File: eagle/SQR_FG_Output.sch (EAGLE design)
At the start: 35 parts, among them IC1 MEGA328P, IC2 NJM7032, IC3 7805T, IC4 TLV1117-33, Q1 16MHz, T1 2SK4017, T2 2SK4017

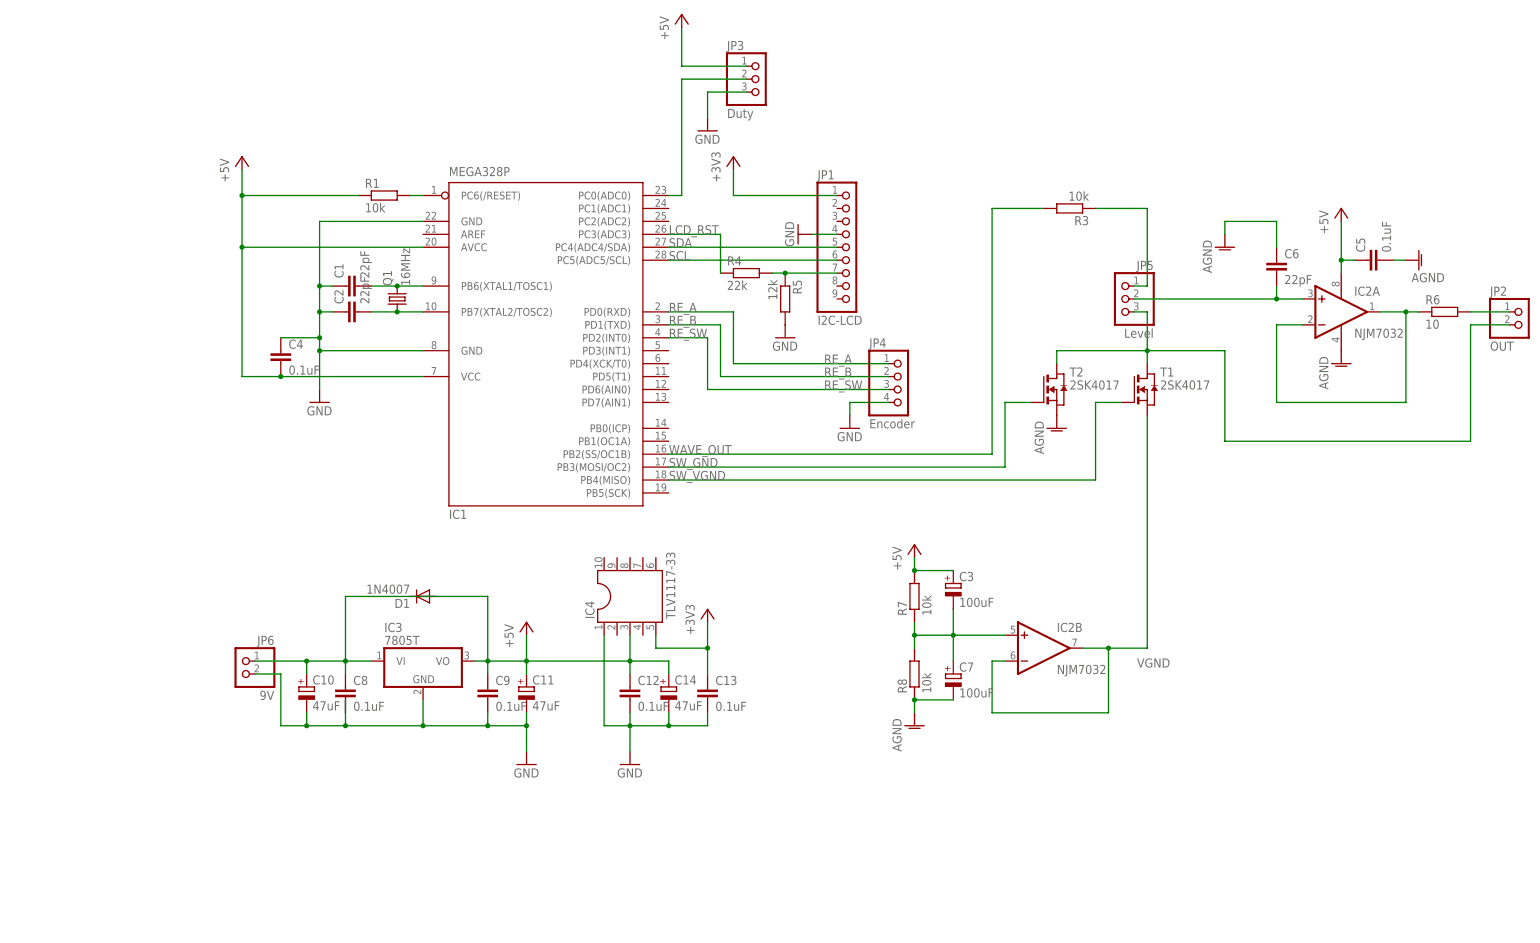
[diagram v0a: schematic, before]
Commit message: eagle files: デジタル部と出力部に基板を分割
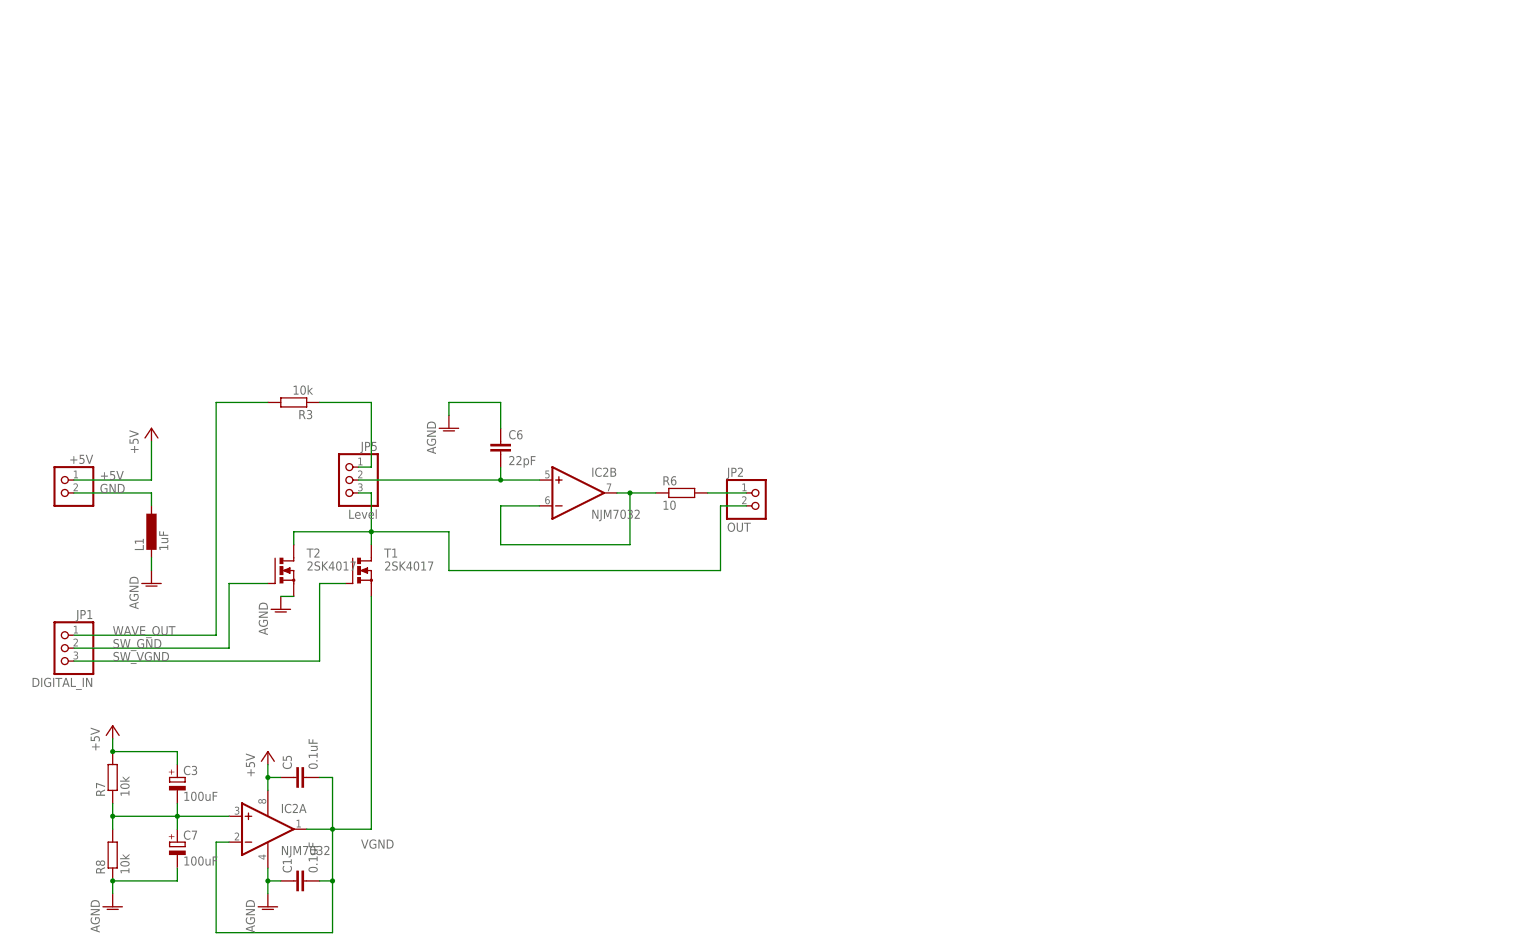
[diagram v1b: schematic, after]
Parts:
- removed C10, C11, C14: 47uF, rcl:CPOL-EUTT2D5L
- removed C12, C13, C4, C8, C9: 0.1uF, rcl:C-EU025-024X044
- removed C2: 22pF, rcl:C-EU025-024X044
- removed D1: 1N4007, diode:1N4004
- removed IC1: MEGA328P, atmel:MEGA8-P
- removed IC3: 7805T, linear:7805T
- removed IC4: TLV1117-33, ic-package:DIL10
- removed JP3: Duty, pinhead:PINHD-1X3
- removed JP4: Encoder, pinhead:PINHD-1X4
- removed JP6: 9V, pinhead:PINHD-1X2
- removed Q1: 16MHz, crystal:CRYSTALHC49S
- removed R1: 10k, rcl:R-EU_0207/7
- removed R4: 22k, rcl:R-EU_0207/7
- removed R5: 12k, rcl:R-EU_0207/7
- added +5V: (no value), pinhead:PINHD-1X2
- added L1: 1uF, rcl:L-EU0204/7
- C1: value 22pF -> 0.1uF
- JP1: value I2C-LCD -> DIGITAL_IN; device pinhead:PINHD-1X9 -> pinhead:PINHD-1X3
- T1, T2: device zetex:NMOSE3L -> transistor-power:RD06HVF1
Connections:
- removed net +3V3: C13.1, IC4.5, JP1.1
- removed net LCD_RST: IC1.PC3(ADC3), R4.1
- removed net N$1: C1.2, IC1.PB6(XTAL1/TOSC1), Q1.2
- removed net N$2: C2.2, IC1.PB7(XTAL2/TOSC2), Q1.1
- removed net N$3: IC1.PC6(/RESET), R1.2
- removed net N$9: IC1.PC0(ADC0), JP3.2
- removed net RE_A: IC1.PD0(RXD), JP4.1
- removed net RE_B: IC1.PD1(TXD), JP4.2
- removed net RE_SW: IC1.PD2(INT0), JP4.3
- removed net RST: JP1.7, R4.2, R5.1
- removed net SCL: IC1.PC5(ADC5/SCL), JP1.6
- removed net SDA: IC1.PC4(ADC4/SDA), JP1.5
- net +5V: now also +5V.1; no longer C10.+, C11.+, C12.1, C14.+, C4.2, C8.1, C9.1, IC1.AVCC, IC1.VCC@1, IC3.VI, IC3.VO, IC4.3, JP3.1, JP6.1, R1.1
- net AGND: now also C1.1, L1.2; no longer C5.2
- net GND: now also +5V.2, L1.1; no longer C1.1, C10.-, C11.-, C12.2, C13.2, C14.-, C2.1, C4.1, C8.2, C9.2, IC1.GND, IC1.GND@1, IC3.GND, IC4.1, JP1.4, JP3.3, JP4.4, JP6.2, R5.2
- net N$15: now also IC2B.+IN; no longer IC2A.+IN
- net N$16: now also IC2B.-IN, IC2B.OUT; no longer IC2A.-IN, IC2A.OUT
- net N$17: now also IC2A.+IN; no longer IC2B.+IN
- net SW_GND: now also JP1.2; no longer IC1.PB3(MOSI/OC2)
- net SW_VGND: now also JP1.3; no longer IC1.PB4(MISO)
- net VGND: now also C1.2, C5.2, IC2A.-IN, IC2A.OUT; no longer IC2B.-IN, IC2B.OUT
- net WAVE_OUT: now also JP1.1; no longer IC1.PB2(SS/OC1B)
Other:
- moved on the sheet: C1, C3, C5, C6, C7, IC2A, IC2B, JP2, JP5, R3, R6, R7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

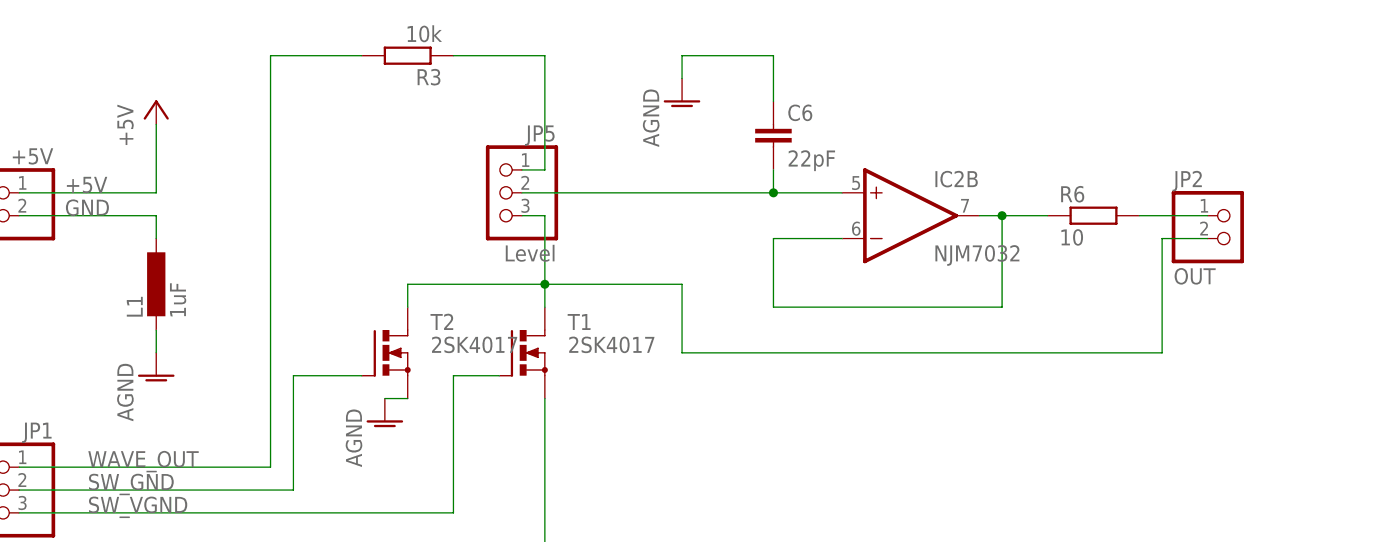
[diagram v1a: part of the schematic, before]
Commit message: SQR_FG_Digital: I2Cの信号をピンソケットで出力できるように変更
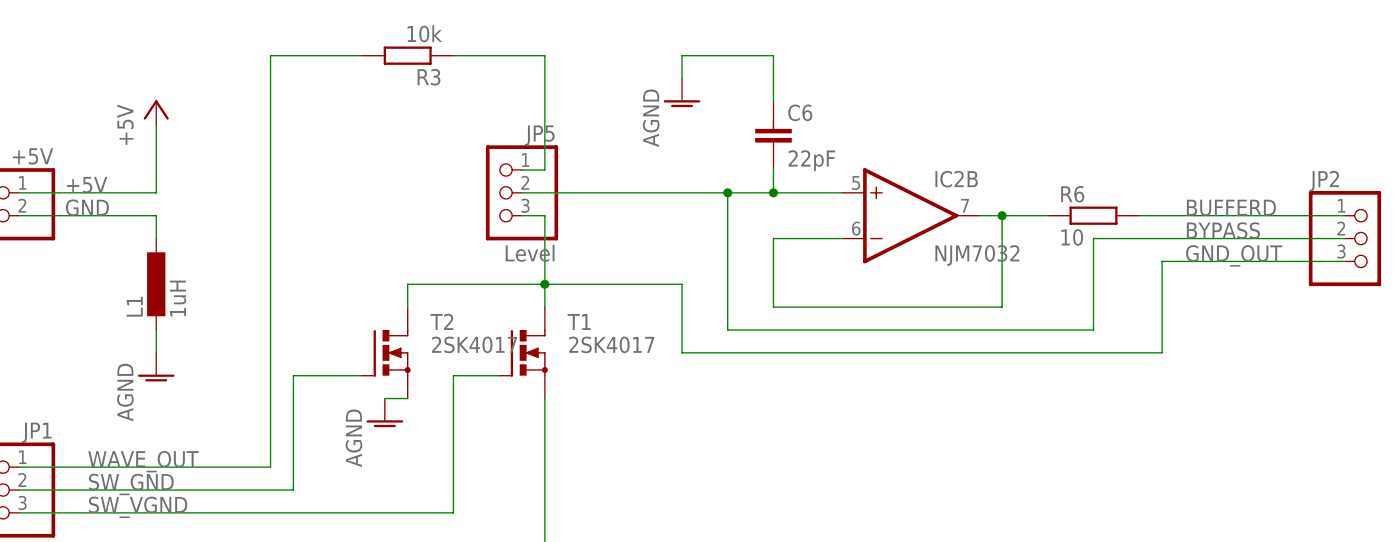
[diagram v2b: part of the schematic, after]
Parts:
- JP2: value OUT -> (none); device pinhead:PINHD-1X2 -> pinhead:PINHD-1X3
- L1: value 1uF -> 1uH
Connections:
- net N$11 renamed BUFFERD
- removed net N$15: C6.2, IC2B.+IN, JP5.2
- removed net N$6: JP2.2, JP5.3, T1.D, T2.D
- new net BYPASS: C6.2, IC2B.+IN, JP2.2, JP5.2
- new net GND_OUT: JP2.3, JP5.3, T1.D, T2.D
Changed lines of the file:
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@@
 <grid distance="0.1" unitdist="inch" unit="inch" style="dots" multiple="1" display="yes" altdistance="0.01" altunitdist="inch" altunit="inch"/>
 <layers>
-<layer number="1" name="Top" color="4" fill="1" visible="yes" active="no"/>
-<layer number="16" name="Bottom" color="1" fill="1" visible="yes" active="no"/>
-<layer number="17" name="Pads" color="2" fill="1" visible="yes" active="no"/>
-<layer number="18" name="Vias" color="2" fill="1" visible="yes" active="no"/>
-<layer number="19" name="Unrouted" color="6" fill="1" visible="yes" active="no"/>
-<layer number="20" name="Dimension" color="15" fill="1" visible="yes" active="no"/>
-<layer number="21" name="tPlace" color="7" fill="1" visible="yes" active="no"/>
-<layer number="22" name="bPlace" color="7" fill="1" visible="yes" active="no"/>
-<layer number="23" name="tOrigins" color="15" fill="1" visible="yes" active="no"/>
-<layer number="24" name="bOrigins" color="15" fill="1" visible="yes" active="no"/>
-<layer number="25" name="tNames" color="7" fill="1" visible="yes" active="no"/>
-<layer number="26" name="bNames" color="7" fill="1" visible="yes" active="no"/>
-<layer number="27" name="tValues" color="7" fill="1" visible="yes" active="no"/>
-<layer number="28" name="bValues" color="7" fill="1" visible="yes" active="no"/>
+<layer number="1" name="Top" color="4" fill="1" visible="no" active="no"/>
+<layer number="16" name="Bottom" color="1" fill="1" visible="no" active="no"/>
+<layer number="17" name="Pads" color="2" fill="1" visible="no" active="no"/>
+<layer number="18" name="Vias" color="2" fill="1" visible="no" active="no"/>
+<layer number="19" name="Unrouted" color="6" fill="1" visible="no" active="no"/>
+<layer number="20" name="Dimension" color="15" fill="1" visible="no" active="no"/>
+<layer number="21" name="tPlace" color="7" fill="1" visible="no" active="no"/>
+<layer number="22" name="bPlace" color="7" fill="1" visible="no" active="no"/>
+<layer number="23" name="tOrigins" color="15" fill="1" visible="no" active="no"/>
+<layer number="24" name="bOrigins" color="15" fill="1" visible="no" active="no"/>
+<layer number="25" name="tNames" color="7" fill="1" visible="no" active="no"/>
+<layer number="26" name="bNames" color="7" fill="1" visible="no" active="no"/>
+<layer number="27" name="tValues" color="7" fill="1" visible="no" active="no"/>
+<layer number="28" name="bValues" color="7" fill="1" visible="no" active="no"/>
 <layer number="29" name="tStop" color="7" fill="3" visible="no" active="no"/>
 <layer number="30" name="bStop" color="7" fill="6" visible="no" active="no"/>
@@
 <layer number="35" name="tGlue" color="7" fill="4" visible="no" active="no"/>
 <layer number="36" name="bGlue" color="7" fill="5" visible="no" active="no"/>
-<layer number="37" name="tTest" color="7" fill="1" visible="yes" active="no"/>
-<layer number="38" name="bTest" color="7" fill="1" visible="yes" active="no"/>
+<layer number="37" name="tTest" color="7" fill="1" visible="no" active="no"/>
+<layer number="38" name="bTest" color="7" fill="1" visible="no" active="no"/>
 <layer number="39" name="tKeepout" color="4" fill="11" visible="no" active="no"/>
 <layer number="40" name="bKeepout" color="1" fill="11" visible="no" active="no"/>
@@
 <layer number="44" name="Drills" color="7" fill="1" visible="no" active="no"/>
 <layer number="45" name="Holes" color="7" fill="1" visible="no" active="no"/>
-<layer number="46" name="Milling" color="3" fill="1" visible="yes" active="no"/>
-<layer number="47" name="Measures" color="7" fill="1" visible="yes" active="no"/>
-<layer number="48" name="Document" color="7" fill="1" visible="yes" active="no"/>
-<layer number="49" name="Reference" color="7" fill="1" visible="yes" active="no"/>
-<layer number="51" name="tDocu" color="7" fill="1" visible="yes" active="no"/>
-<layer number="52" name="bDocu" color="7" fill="1" visible="yes" active="no"/>
+<layer number="46" name="Milling" color="3" fill="1" visible="no" active="no"/>
+<layer number="47" name="Measures" color="7" fill="1" visible="no" active="no"/>
+<layer number="48" name="Document" color="7" fill="1" visible="no" active="no"/>
+<layer number="49" name="Reference" color="7" fill="1" visible="no" active="no"/>
+<layer number="51" name="tDocu" color="7" fill="1" visible="no" active="no"/>
+<layer number="52" name="bDocu" color="7" fill="1" visible="no" active="no"/>
 <layer number="90" name="Modules" color="5" fill="1" visible="yes" active="yes"/>
 <layer number="91" name="Nets" color="2" fill="1" visible="yes" active="yes"/>
@@
 <part name="T2" library="transistor-power" deviceset="RD06HVF1" device="" value="2SK4017"/>
 <part name="C5" library="rcl" deviceset="C-EU" device="025-024X044" value="0.1uF"/>
-<part name="JP2" library="pinhead" deviceset="PINHD-1X2" device="" value="OUT"/>
 <part name="R3" library="rcl" deviceset="R-EU_" device="0207/7" value="10k"/>
 <part name="C6" library="rcl" deviceset="C-EU" device="025-024X044" value="22pF"/>
@@
 <part name="+5V" library="pinhead" deviceset="PINHD-1X2" device=""/>
 <part name="P+1" library="supply1" deviceset="+5V" device=""/>
-<part name="L1" library="rcl" deviceset="L-EU" device="0204/7" value="1uF"/>
+<part name="L1" library="rcl" deviceset="L-EU" device="0204/7" value="1uH"/>
 <part name="AGND4" library="supply1" deviceset="AGND" device=""/>
+<part name="JP2" library="pinhead" deviceset="PINHD-1X3" device=""/>
 </parts>
 <sheets>
@@
 <instance part="T2" gate="G$1" x="12.7" y="43.18"/>
 <instance part="C5" gate="G$1" x="15.24" y="2.54" rot="R90"/>
-<instance part="JP2" gate="G$1" x="106.68" y="55.88"/>
 <instance part="R3" gate="G$1" x="15.24" y="76.2" rot="R180"/>
 <instance part="C6" gate="G$1" x="55.88" y="68.58"/>
@@
 <instance part="L1" gate="G$1" x="-12.7" y="50.8"/>
 <instance part="AGND4" gate="VR1" x="-12.7" y="40.64"/>
+<instance part="JP2" gate="A" x="121.92" y="55.88"/>
 </instances>
 <busses>
@@
 </segment>
 </net>
-<net name="N$11" class="0">
+<net name="BUFFERD" class="0">
 <segment>
 <pinref part="R6" gate="G$1" pin="2"/>
-<wire x1="96.52" y1="58.42" x2="104.14" y2="58.42" width="0.1524" layer="91"/>
-<pinref part="JP2" gate="G$1" pin="1"/>
+<wire x1="96.52" y1="58.42" x2="119.38" y2="58.42" width="0.1524" layer="91"/>
+<pinref part="JP2" gate="A" pin="1"/>
+<label x="101.6" y="58.42" size="1.778" layer="95"/>
 </segment>
 </net>
@@
 </segment>
 </net>
-<net name="N$6" class="0">
+<net name="GND_OUT" class="0">
 <segment>
 <pinref part="T1" gate="G$1" pin="D"/>
@@
 <wire x1="45.72" y1="50.8" x2="45.72" y2="43.18" width="0.1524" layer="91"/>
 <wire x1="45.72" y1="43.18" x2="99.06" y2="43.18" width="0.1524" layer="91"/>
-<wire x1="99.06" y1="43.18" x2="99.06" y2="55.88" width="0.1524" layer="91"/>
-<pinref part="JP2" gate="G$1" pin="2"/>
-<wire x1="104.14" y1="55.88" x2="99.06" y2="55.88" width="0.1524" layer="91"/>
+<wire x1="99.06" y1="43.18" x2="99.06" y2="53.34" width="0.1524" layer="91"/>
 <pinref part="JP5" gate="A" pin="3"/>
 <wire x1="27.94" y1="58.42" x2="30.48" y2="58.42" width="0.1524" layer="91"/>
+<pinref part="JP2" gate="A" pin="3"/>
+<wire x1="119.38" y1="53.34" x2="99.06" y2="53.34" width="0.1524" layer="91"/>
+<label x="101.6" y="53.34" size="1.778" layer="95"/>
 </segment>
 </net>
@@
 </segment>
 </net>
-<net name="N$15" class="0">
-<segment>
-<wire x1="27.94" y1="60.96" x2="55.88" y2="60.96" width="0.1524" layer="91"/>
+<net name="BYPASS" class="0">
+<segment>
+<wire x1="27.94" y1="60.96" x2="50.8" y2="60.96" width="0.1524" layer="91"/>
 <pinref part="C6" gate="G$1" pin="2"/>
+<wire x1="50.8" y1="60.96" x2="55.88" y2="60.96" width="0.1524" layer="91"/>
 <wire x1="55.88" y1="63.5" x2="55.88" y2="60.96" width="0.1524" layer="91"/>
 <pinref part="JP5" gate="A" pin="2"/>
@@
 <wire x1="63.5" y1="60.96" x2="55.88" y2="60.96" width="0.1524" layer="91"/>
 <junction x="55.88" y="60.96"/>
-</segment>
-</net>
+<pinref part="JP2" gate="A" pin="2"/>
+<wire x1="119.38" y1="55.88" x2="91.44" y2="55.88" width="0.1524" layer="91"/>
+<wire x1="91.44" y1="55.88" x2="91.44" y2="45.72" width="0.1524" layer="91"/>
+<wire x1="91.44" y1="45.72" x2="50.8" y2="45.72" width="0.1524" layer="91"/>
+<wire x1="50.8" y1="45.72" x2="50.8" y2="60.96" width="0.1524" layer="91"/>
+<junction x="50.8" y="60.96"/>
+<label x="101.6" y="55.88" size="1.778" layer="95"/>
+</segment>
+</net>
